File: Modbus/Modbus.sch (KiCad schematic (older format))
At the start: 9 parts, among them J1 CONN_01X03, J2 DB9_Male, Q1 BSS123, U1 MAX481E

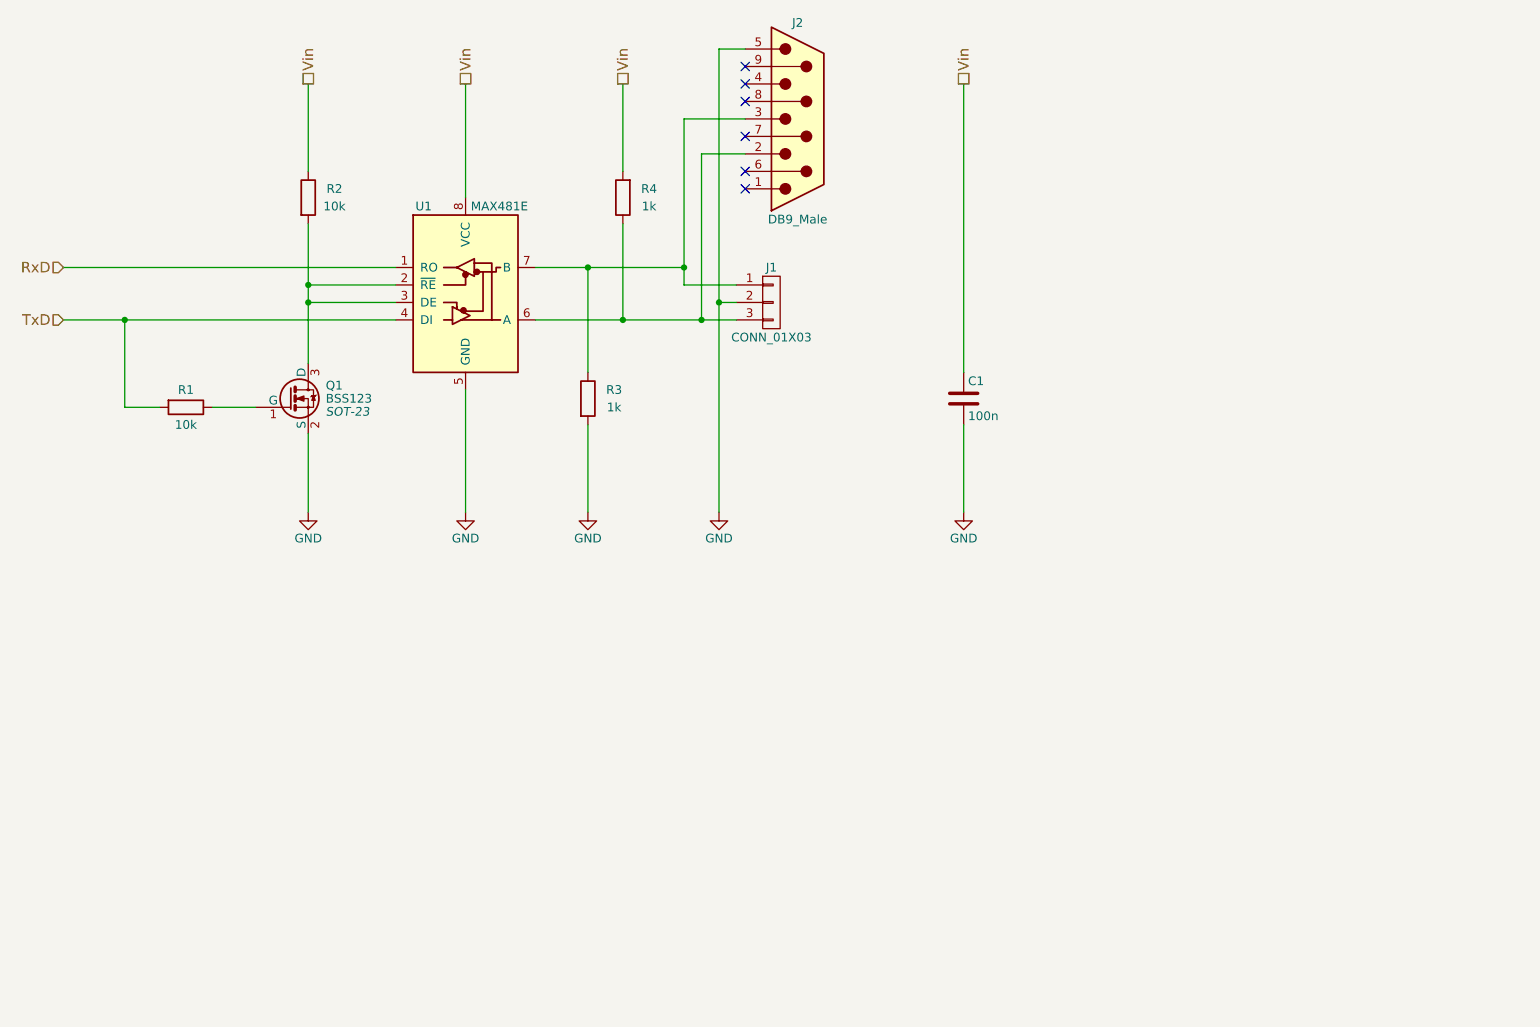
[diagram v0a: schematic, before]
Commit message: added CreativeCommons License
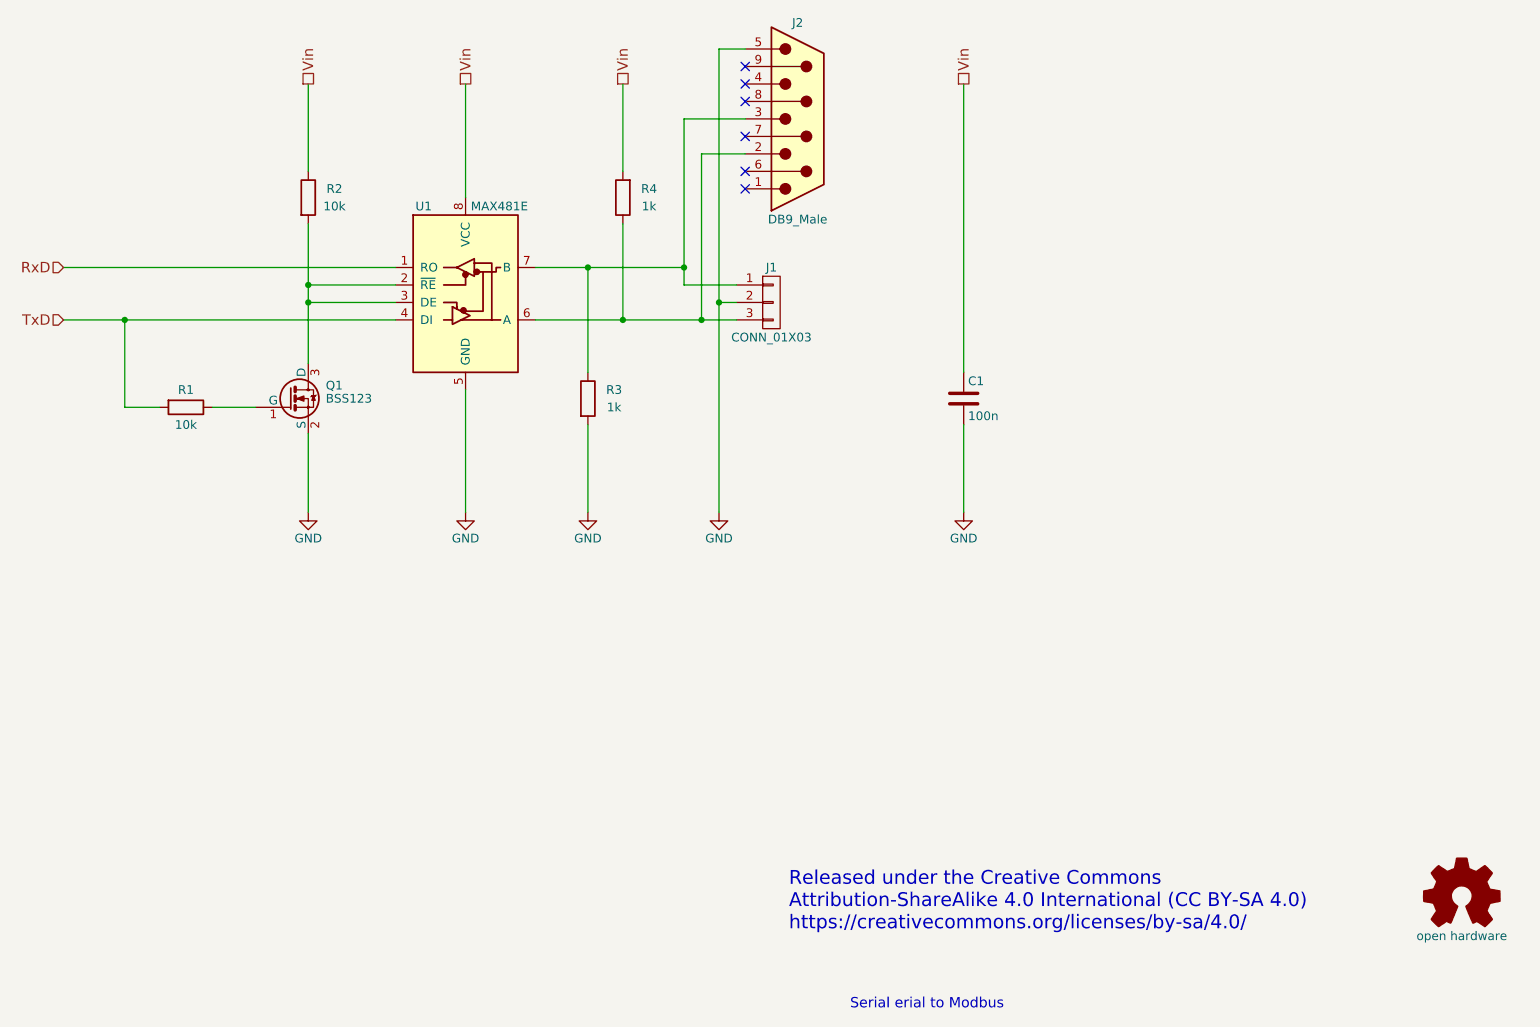
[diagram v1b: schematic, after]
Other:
- note added: "Released under the Creative Commons\nAttribution-ShareAlike 4.0 International (CC BY-SA 4.0) \nhttps://creativecommons.org/licenses/by-sa/4.0/"
- note added: "Serial erial to Modbus"
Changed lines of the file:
@@
 LIBS:contrib
 LIBS:valves
+LIBS:graphic_symbols
 LIBS:Modbus-cache
 EELAYER 25 0
@@
 F 0 "Q1" H 4400 4075 50  0000 L CNN
 F 1 "BSS123" H 4400 4000 50  0000 L CNN
-F 2 "SOT-23" H 4400 3925 50  0000 L CIN
+F 2 "SOT-23" H 4400 3925 50  0001 L CIN
 F 3 "" H 4200 4000 50  0000 L CNN
 	1    4200 4000
@@
 Wire Wire Line
 	8050 3850 8050 2200
+Text Notes 7050 7050 0    79   ~ 0
+Released under the Creative Commons\nAttribution-ShareAlike 4.0 International (CC BY-SA 4.0) \nhttps://creativecommons.org/licenses/by-sa/4.0/
+$Comp
+L Logo_Open_Hardware_Small #LOGO?
+U 1 1 59A1FA02
+P 10900 6850
+F 0 "#LOGO?" H 10900 7125 50  0001 C CNN
+F 1 "open hardware" H 10900 6625 50  0000 C CNN
+F 2 "" H 10900 6850 50  0001 C CNN
+F 3 "" H 10900 6850 50  0001 C CNN
+	1    10900 6850
+	1    0    0    -1
+$EndComp
+Text Notes 7400 7500 0    59   ~ 0
+Serial erial to Modbus
 $EndSCHEMATC
